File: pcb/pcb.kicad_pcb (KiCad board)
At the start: 2 copper layers, 60 x 45 mm, 15 parts

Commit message: Add makefile for order automation
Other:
- board text added: "Dog Fence Indicator 1.0.1"
- board text removed: "Dog Fence Indicator 1.0"

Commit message: v1.0.2 thanks to Kimi K3, cleanup LED_C pin semantics and docs
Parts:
- J_LED_A, J_LED_C: value KF129S-5.08-2P -> KF129-5.08-2P
- turned J_LED_C to 90 degrees
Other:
- board text added: "Dog Fence Indicator 1.0.2"
- board text removed: "Dog Fence Indicator 1.0.1"
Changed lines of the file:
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@@
 				(thickness 0.01)
 			)
-			(layer "F.Cu"
-				(type "copper")
-				(thickness 0.035)
-			)
+		(layer "F.Cu"
+			(type "copper")
+			(thickness 0.07)
+		)
 			(layer "dielectric 1"
 				(type "core")
@@
 				(loss_tangent 0.02)
 			)
-			(layer "B.Cu"
-				(type "copper")
-				(thickness 0.035)
-			)
+		(layer "B.Cu"
+			(type "copper")
+			(thickness 0.07)
+		)
 			(layer "B.Mask"
 				(type "Bottom Solder Mask")
@@
 			)
 		)
-		(property "Value" "KF129S-5.08-2P"
+		(property "Value" "KF129-5.08-2P"
 			(at 0 0 0)
 			(layer "F.Fab")
@@
 	(footprint "TerminalBlock_Phoenix:TerminalBlock_Phoenix_MKDS-1,5-2-5.08_1x02_P5.08mm_Horizontal"
 		(layer "F.Cu")
-		(at 144 138.5 -90)
+		(at 144 138.5 90)
 		(property "Reference" "J_LED_C"
 			(at 0 0 0)
@@
 			)
 		)
-		(property "Value" "KF129S-5.08-2P"
+		(property "Value" "KF129-5.08-2P"
 			(at 0 0 0)
 			(layer "F.Fab")
@@
 		)
 		(property "Datasheet" ""
-			(at 0 0 270)
+			(at 0 0 90)
 			(layer "F.Fab")
 			(hide yes)
@@
 		)
 		(property "Description" ""
-			(at 0 0 270)
+			(at 0 0 90)
 			(layer "F.Fab")
 			(hide yes)
@@
 		)
 		(pad "1" thru_hole roundrect
-			(at 0 -2.54 270)
+			(at 0 -2.54 90)
 			(size 2.8 2.8)
 			(drill 1.3)
@@
 		)
 		(pad "2" thru_hole circle
-			(at 0 2.54 270)
+			(at 0 2.54 90)
 			(size 2.8 2.8)
 			(drill 1.3)
@@
 		)
 	)
-	(gr_text "Dog Fence Indicator 1.0.1"
+	(gr_text "Dog Fence Indicator 1.0.2"
 		(at 122.2 102.3 0)
 		(layer "F.SilkS")

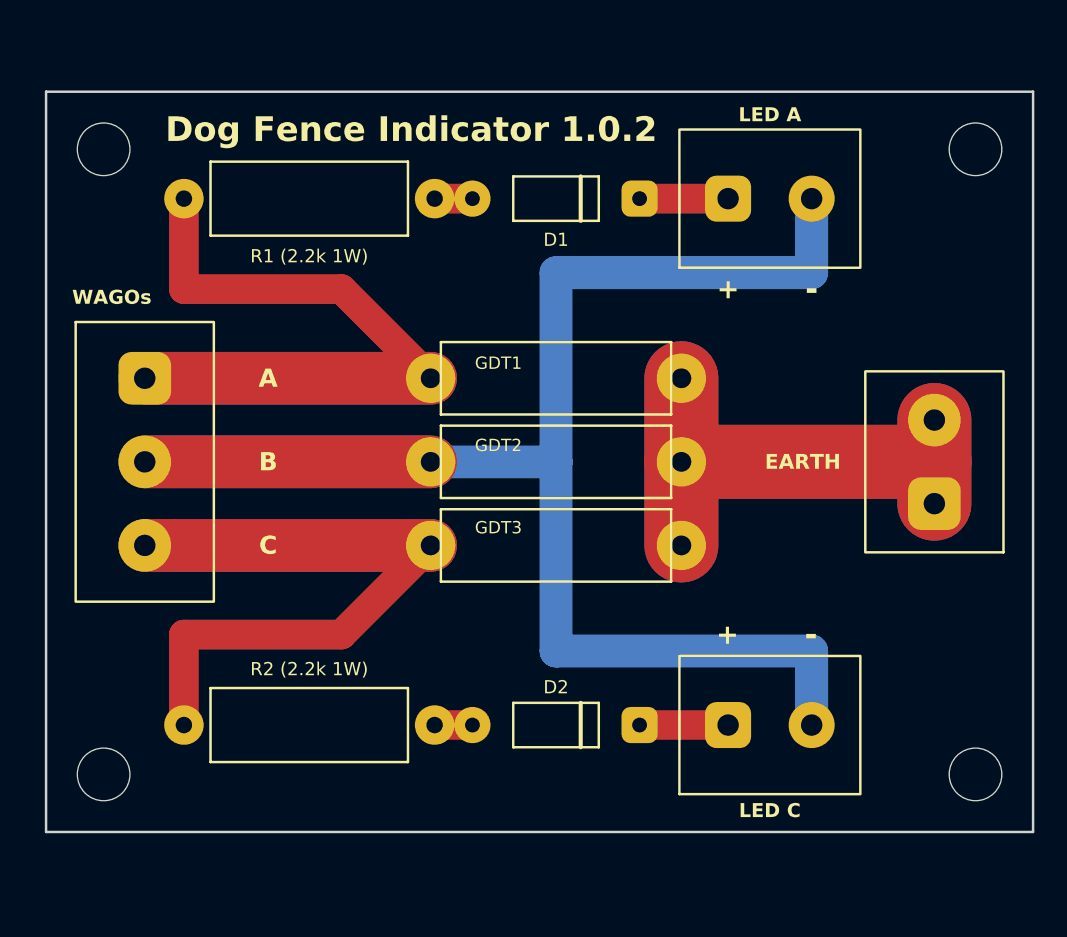
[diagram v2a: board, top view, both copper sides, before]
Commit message: Gemini 3.8 Flash improvements to GDT locations and completeness
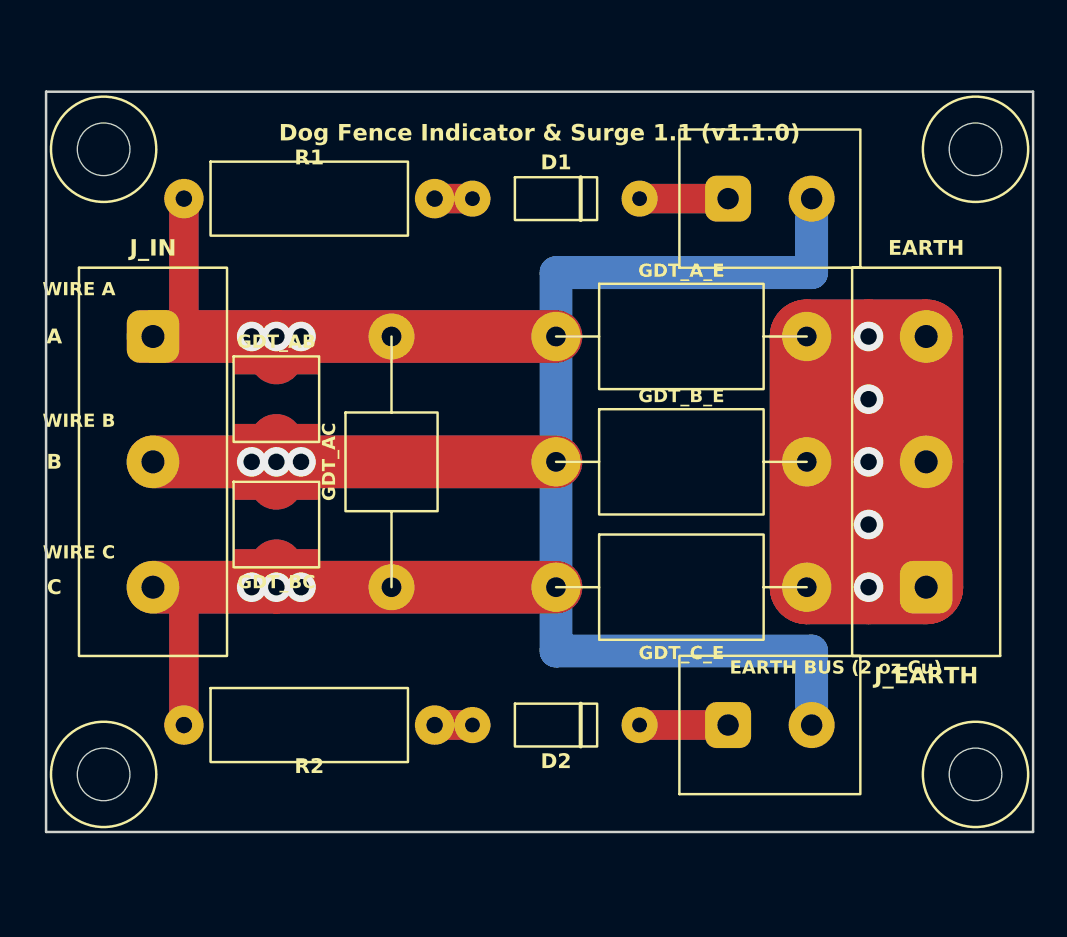
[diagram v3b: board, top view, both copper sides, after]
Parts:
- removed GDT1, GDT2, GDT3: 2R470TD-8, Resistor_THT:R_Axial_DIN0617_L17.0mm_D6.0mm_P20.32mm_Horizontal
- removed the J_EARTH at (154.0, 122.5)
- removed the J_IN at (106.0, 122.5)
- removed R1 (2.2k 1W): 2.2k 1W, Resistor_THT:R_Axial_DIN0414_L11.9mm_D4.5mm_P15.24mm_Horizontal
- removed R2 (2.2k 1W): 2.2k 1W, Resistor_THT:R_Axial_DIN0414_L11.9mm_D4.5mm_P15.24mm_Horizontal
- added GDT_AB: SMD5050-470NA, GDT_SMD:GDT_SMD_5.0x5.0mm, F.Cu at (114.0, 118.7)
- added GDT_AC: 2RA470-L5.5, Resistor_THT:R_Axial_DIN0617_L17.0mm_D6.0mm_P15.24mm_Horizontal, F.Cu at (121.0, 122.5)
- added GDT_A_E: 2R470TD-8, Resistor_THT:R_Axial_DIN0617_L17.0mm_D6.0mm_P15.24mm_Horizontal, F.Cu at (138.6, 114.9)
- added GDT_BC: SMD5050-470NA, GDT_SMD:GDT_SMD_5.0x5.0mm, F.Cu at (114.0, 126.3)
- added GDT_B_E: 2R470TD-8, Resistor_THT:R_Axial_DIN0617_L17.0mm_D6.0mm_P15.24mm_Horizontal, F.Cu at (138.6, 122.5)
- added GDT_C_E: 2R470TD-8, Resistor_THT:R_Axial_DIN0617_L17.0mm_D6.0mm_P15.24mm_Horizontal, F.Cu at (138.6, 130.1)
- added J_EARTH: KF128-7.62-3P, TerminalBlock_Phoenix:TerminalBlock_Phoenix_MKDS-1,5-3-7.62_1x03_P7.62mm_Horizontal, F.Cu at (153.5, 122.5)
- added J_IN: KF128-7.62-3P, TerminalBlock_Phoenix:TerminalBlock_Phoenix_MKDS-1,5-3-7.62_1x03_P7.62mm_Horizontal, F.Cu at (106.5, 122.5)
- added R1: 2.2k 1W, Resistor_THT:R_Axial_DIN0414_L11.9mm_D4.5mm_P15.24mm_Horizontal, F.Cu at (116.0, 106.5)
- added R2: 2.2k 1W, Resistor_THT:R_Axial_DIN0414_L11.9mm_D4.5mm_P15.24mm_Horizontal, F.Cu at (116.0, 138.5)
- H1, H2, H3, H4: value M3 -> MountingHole_3.2mm_M3
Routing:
- net EARTH: track 61.2 -> 135.0 mm, vias 0 -> 5
- net WIRE_B: track 105.5 -> 114.7 mm, vias 0 -> 3
- net WIRE_C: track 57.5 -> 58.7 mm, vias 0 -> 3
- net WIRE_A: track 57.5 -> 58.7 mm, vias 0 -> 3
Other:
- board text added: "Dog Fence Indicator & Surge 1.1 (v1.1.0)"
- board text added: "EARTH BUS (2 oz Cu)"
- board text added: "WIRE A"
- board text added: "WIRE B"
- board text added: "WIRE C"
- board text removed: "+"
- board text removed: "-"
- board text removed: "A"
- board text removed: "B"
- board text removed: "C"
- board text removed: "Dog Fence Indicator 1.0.2"
- board text removed: "EARTH"
- board text removed: "LED A"
- board text removed: "LED C"
- board text removed: "WAGOs"

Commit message: Avoid short on back side Wire B return and wires A&C. Gemini 3.8 Flash.
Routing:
- net WIRE_B: track 114.7 -> 107.1 mm
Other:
- board text added: "+"
- board text added: "-"
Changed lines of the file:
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@@
 		(property "Value" "KF129-5.08-2P" (at 0 0 0) (layer "F.Fab") (hide yes) (effects (font (size 1 1) (thickness 0.15))))
 		(fp_rect (start -4.2 -5.5) (end 4.2 5.5) (stroke (width 0.15) (type solid)) (fill no) (layer "F.SilkS"))
-		(pad "1" thru_hole roundrect (at 0 -2.54 90) (size 2.8 2.8) (drill 1.3) (layers "*.Cu" "*.Mask") (roundrect_rratio 0.25) (net 6 "LED_A_POS"))
-		(pad "2" thru_hole circle (at 0 2.54 90) (size 2.8 2.8) (drill 1.3) (layers "*.Cu" "*.Mask") (net 2 "WIRE_B"))
+		(pad "1" thru_hole roundrect (at 0 2.54 90) (size 2.8 2.8) (drill 1.3) (layers "*.Cu" "*.Mask") (roundrect_rratio 0.25) (net 6 "LED_A_POS"))
+		(pad "2" thru_hole circle (at 0 -2.54 90) (size 2.8 2.8) (drill 1.3) (layers "*.Cu" "*.Mask") (net 2 "WIRE_B"))
 	)
 	(footprint "TerminalBlock_Phoenix:TerminalBlock_Phoenix_MKDS-1,5-2-5.08_1x02_P5.08mm_Horizontal"
@@
 		(property "Value" "KF129-5.08-2P" (at 0 0 0) (layer "F.Fab") (hide yes) (effects (font (size 1 1) (thickness 0.15))))
 		(fp_rect (start -4.2 -5.5) (end 4.2 5.5) (stroke (width 0.15) (type solid)) (fill no) (layer "F.SilkS"))
-		(pad "1" thru_hole roundrect (at 0 -2.54 90) (size 2.8 2.8) (drill 1.3) (layers "*.Cu" "*.Mask") (roundrect_rratio 0.25) (net 8 "LED_C_POS") (uuid "84165048-PAD1"))
-		(pad "2" thru_hole circle (at 0 2.54 90) (size 2.8 2.8) (drill 1.3) (layers "*.Cu" "*.Mask") (net 2 "WIRE_B") (uuid "84165048-PAD2"))
+		(pad "1" thru_hole roundrect (at 0 2.54 90) (size 2.8 2.8) (drill 1.3) (layers "*.Cu" "*.Mask") (roundrect_rratio 0.25) (net 8 "LED_C_POS") (uuid "84165048-PAD1"))
+		(pad "2" thru_hole circle (at 0 -2.54 90) (size 2.8 2.8) (drill 1.3) (layers "*.Cu" "*.Mask") (net 2 "WIRE_B") (uuid "84165048-PAD2"))
 	)
 	(footprint "Resistor_THT:R_Axial_DIN0414_L11.9mm_D4.5mm_P15.24mm_Horizontal"
@@
 	(gr_text "WIRE C" (at 102 128 0) (layer "F.SilkS") (uuid "LBL-C") (effects (font (size 0.8 0.8) (thickness 0.12) (bold yes))))
 	(gr_text "EARTH BUS (2 oz Cu)" (at 148 135 0) (layer "F.SilkS") (uuid "LBL-EARTH") (effects (font (size 0.8 0.8) (thickness 0.12) (bold yes))))
+	(gr_text "+" (at 141.46 103.0 0) (layer "F.SilkS") (uuid "TXT-LED-A-POS") (effects (font (size 1.2 1.2) (thickness 0.18) (bold yes))))
+	(gr_text "-" (at 146.54 103.0 0) (layer "F.SilkS") (uuid "TXT-LED-A-NEG") (effects (font (size 1.2 1.2) (thickness 0.18) (bold yes))))
+	(gr_text "+" (at 141.46 142.0 0) (layer "F.SilkS") (uuid "TXT-LED-C-POS") (effects (font (size 1.2 1.2) (thickness 0.18) (bold yes))))
+	(gr_text "-" (at 146.54 142.0 0) (layer "F.SilkS") (uuid "TXT-LED-C-NEG") (effects (font (size 1.2 1.2) (thickness 0.18) (bold yes))))
 	(via (at 112.5 114.88) (size 1.8) (drill 1.0) (layers "F.Cu" "B.Cu") (net 1) (uuid "VIA-A-1"))
 	(via (at 114.0 114.88) (size 1.8) (drill 1.0) (layers "F.Cu" "B.Cu") (net 1) (uuid "VIA-A-2"))
@@
 	(segment (start 114.0 122.50) (end 114.0 121.19) (width 3.2) (layer "F.Cu") (net 2) (uuid "TRK-B-SMD1"))
 	(segment (start 114.0 122.50) (end 114.0 123.81) (width 3.2) (layer "F.Cu") (net 2) (uuid "TRK-B-SMD2"))
-	(segment (start 131.0 122.50) (end 131.0 111.0) (width 2.0) (layer "B.Cu") (net 2) (uuid "TRK-B-B2"))
-	(segment (start 131.0 111.0) (end 146.54 111.0) (width 2.0) (layer "B.Cu") (net 2) (uuid "TRK-B-B3"))
-	(segment (start 146.54 111.0) (end 146.54 106.5) (width 2.0) (layer "B.Cu") (net 2) (uuid "TRK-B-B4"))
-	(segment (start 131.0 122.50) (end 131.0 134.0) (width 2.0) (layer "B.Cu") (net 2) (uuid "TRK-B-B5"))
-	(segment (start 131.0 134.0) (end 146.54 134.0) (width 2.0) (layer "B.Cu") (net 2) (uuid "TRK-B-B6"))
-	(segment (start 146.54 134.0) (end 146.54 138.5) (width 2.0) (layer "B.Cu") (net 2) (uuid "TRK-B-B7"))
+	(segment (start 131.0 122.50) (end 138.62 122.50) (width 2.0) (layer "B.Cu") (net 2) (uuid "TRK-B-B2A"))
+	(segment (start 138.62 122.50) (end 138.62 110.20) (width 1.6) (layer "B.Cu") (net 2) (uuid "TRK-B-B2B"))
+	(segment (start 138.62 110.20) (end 146.54 110.20) (width 1.5) (layer "B.Cu") (net 2) (uuid "TRK-B-B3"))
+	(segment (start 146.54 110.20) (end 146.54 106.50) (width 1.5) (layer "B.Cu") (net 2) (uuid "TRK-B-B4"))
+	(segment (start 138.62 122.50) (end 138.62 134.80) (width 1.6) (layer "B.Cu") (net 2) (uuid "TRK-B-B5B"))
+	(segment (start 138.62 134.80) (end 146.54 134.80) (width 1.5) (layer "B.Cu") (net 2) (uuid "TRK-B-B6"))
+	(segment (start 146.54 134.80) (end 146.54 138.50) (width 1.5) (layer "B.Cu") (net 2) (uuid "TRK-B-B7"))
 	(segment (start 106.5 130.12) (end 131.0 130.12) (width 3.2) (layer "F.Cu") (net 3) (uuid "TRK-C-F1"))
 	(segment (start 106.5 130.12) (end 131.0 130.12) (width 3.2) (layer "B.Cu") (net 3) (uuid "TRK-C-B1"))

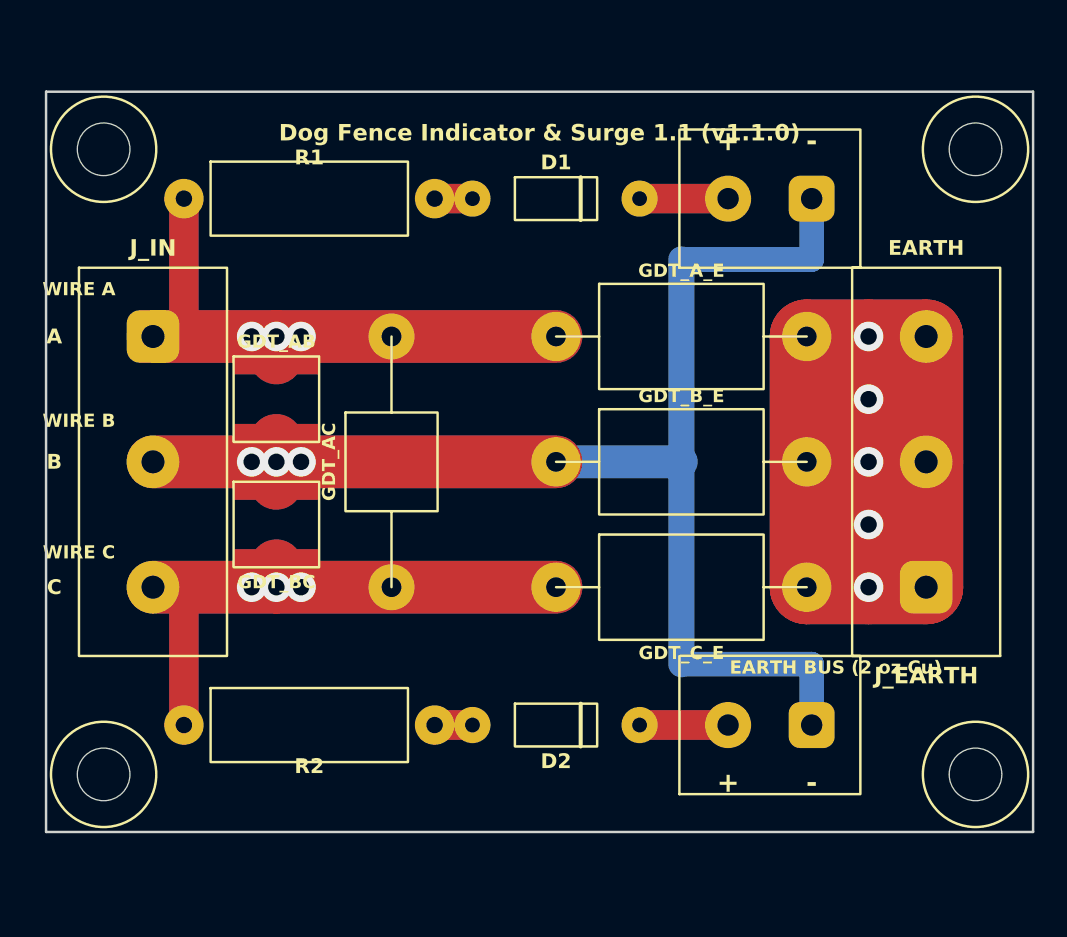
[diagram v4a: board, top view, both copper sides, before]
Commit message: Addressed surge flash concern between Wire B returns and EARTH on the back side
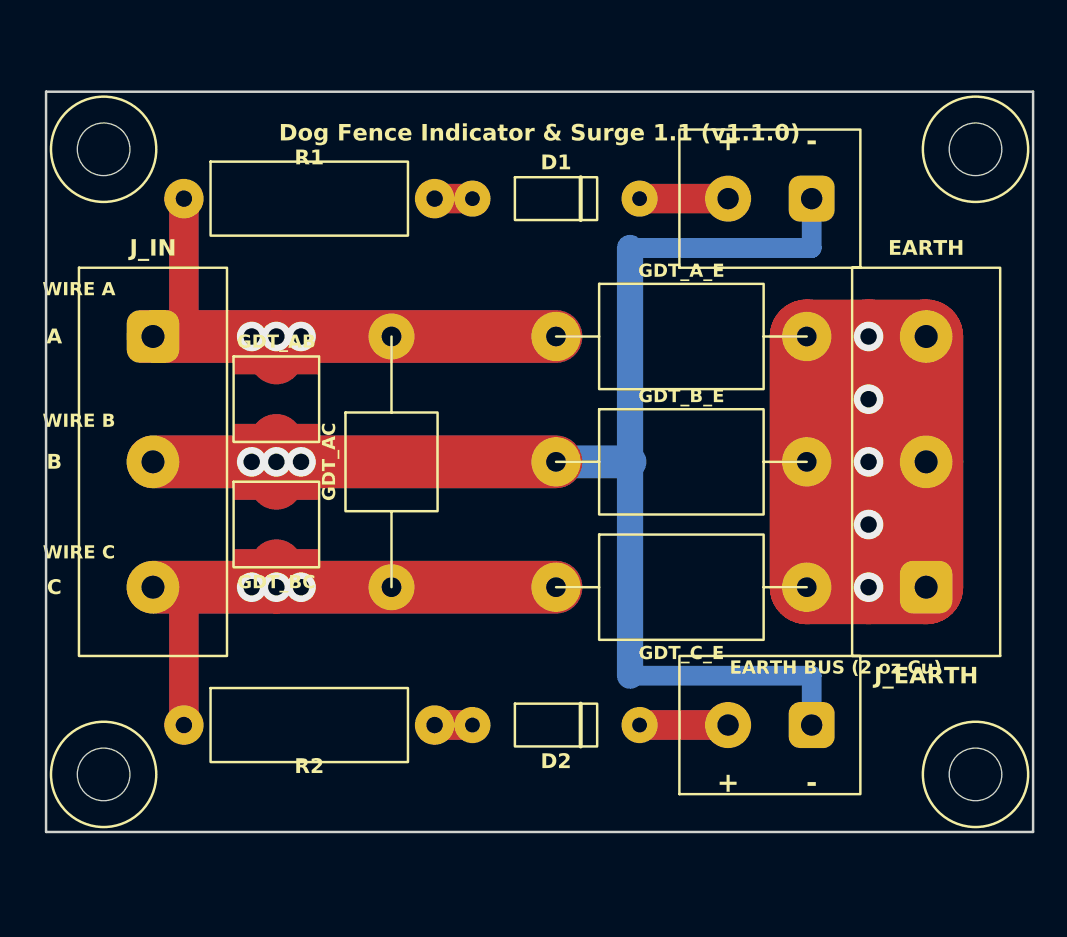
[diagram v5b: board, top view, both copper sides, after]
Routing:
- net WIRE_B: track 107.1 -> 110.2 mm
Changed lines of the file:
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@@
 	(segment (start 114.0 122.50) (end 114.0 121.19) (width 3.2) (layer "F.Cu") (net 2) (uuid "TRK-B-SMD1"))
 	(segment (start 114.0 122.50) (end 114.0 123.81) (width 3.2) (layer "F.Cu") (net 2) (uuid "TRK-B-SMD2"))
-	(segment (start 131.0 122.50) (end 138.62 122.50) (width 2.0) (layer "B.Cu") (net 2) (uuid "TRK-B-B2A"))
-	(segment (start 138.62 122.50) (end 138.62 110.20) (width 1.6) (layer "B.Cu") (net 2) (uuid "TRK-B-B2B"))
-	(segment (start 138.62 110.20) (end 146.54 110.20) (width 1.5) (layer "B.Cu") (net 2) (uuid "TRK-B-B3"))
-	(segment (start 146.54 110.20) (end 146.54 106.50) (width 1.5) (layer "B.Cu") (net 2) (uuid "TRK-B-B4"))
-	(segment (start 138.62 122.50) (end 138.62 134.80) (width 1.6) (layer "B.Cu") (net 2) (uuid "TRK-B-B5B"))
-	(segment (start 138.62 134.80) (end 146.54 134.80) (width 1.5) (layer "B.Cu") (net 2) (uuid "TRK-B-B6"))
-	(segment (start 146.54 134.80) (end 146.54 138.50) (width 1.5) (layer "B.Cu") (net 2) (uuid "TRK-B-B7"))
+	(segment (start 131.0 122.50) (end 135.50 122.50) (width 2.0) (layer "B.Cu") (net 2) (uuid "TRK-B-B2A"))
+	(segment (start 135.50 122.50) (end 135.50 109.50) (width 1.6) (layer "B.Cu") (net 2) (uuid "TRK-B-B2B"))
+	(segment (start 135.50 109.50) (end 146.54 109.50) (width 1.2) (layer "B.Cu") (net 2) (uuid "TRK-B-B3"))
+	(segment (start 146.54 109.50) (end 146.54 106.50) (width 1.2) (layer "B.Cu") (net 2) (uuid "TRK-B-B4"))
+	(segment (start 135.50 122.50) (end 135.50 135.50) (width 1.6) (layer "B.Cu") (net 2) (uuid "TRK-B-B5B"))
+	(segment (start 135.50 135.50) (end 146.54 135.50) (width 1.2) (layer "B.Cu") (net 2) (uuid "TRK-B-B6"))
+	(segment (start 146.54 135.50) (end 146.54 138.50) (width 1.2) (layer "B.Cu") (net 2) (uuid "TRK-B-B7"))
 	(segment (start 106.5 130.12) (end 131.0 130.12) (width 3.2) (layer "F.Cu") (net 3) (uuid "TRK-C-F1"))
 	(segment (start 106.5 130.12) (end 131.0 130.12) (width 3.2) (layer "B.Cu") (net 3) (uuid "TRK-C-B1"))
@@
 	(segment (start 108.38 130.12) (end 108.38 138.5) (width 1.8) (layer "F.Cu") (net 3) (uuid "TRK-C-F2"))
 	(segment (start 146.24 114.88) (end 146.24 130.12) (width 4.5) (layer "F.Cu") (net 4) (uuid "TRK-E-F1"))
-	(segment (start 146.24 114.88) (end 146.24 130.12) (width 4.5) (layer "B.Cu") (net 4) (uuid "TRK-E-B1"))
+	(segment (start 146.24 114.88) (end 146.24 130.12) (width 3.0) (layer "B.Cu") (net 4) (uuid "TRK-E-B1"))
 	(segment (start 146.24 114.88) (end 153.5 114.88) (width 4.5) (layer "F.Cu") (net 4) (uuid "TRK-E-F2"))
-	(segment (start 146.24 114.88) (end 153.5 114.88) (width 4.5) (layer "B.Cu") (net 4) (uuid "TRK-E-B2"))
+	(segment (start 146.24 114.88) (end 153.5 114.88) (width 3.0) (layer "B.Cu") (net 4) (uuid "TRK-E-B2"))
 	(segment (start 146.24 122.50) (end 153.5 122.50) (width 4.5) (layer "F.Cu") (net 4) (uuid "TRK-E-F3"))
 	(segment (start 146.24 122.50) (end 153.5 122.50) (width 4.5) (layer "B.Cu") (net 4) (uuid "TRK-E-B3"))
 	(segment (start 146.24 130.12) (end 153.5 130.12) (width 4.5) (layer "F.Cu") (net 4) (uuid "TRK-E-F4"))
-	(segment (start 146.24 130.12) (end 153.5 130.12) (width 4.5) (layer "B.Cu") (net 4) (uuid "TRK-E-B4"))
+	(segment (start 146.24 130.12) (end 153.5 130.12) (width 3.0) (layer "B.Cu") (net 4) (uuid "TRK-E-B4"))
 	(segment (start 150.0 114.88) (end 150.0 130.12) (width 4.5) (layer "F.Cu") (net 4) (uuid "TRK-E-F6"))
 	(segment (start 150.0 114.88) (end 150.0 130.12) (width 4.5) (layer "B.Cu") (net 4) (uuid "TRK-E-B6"))
